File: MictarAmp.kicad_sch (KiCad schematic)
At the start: 8 parts, among them J1 AudioJack3, J2 AudioJack4, J3 AudioJack2, U1 LM386

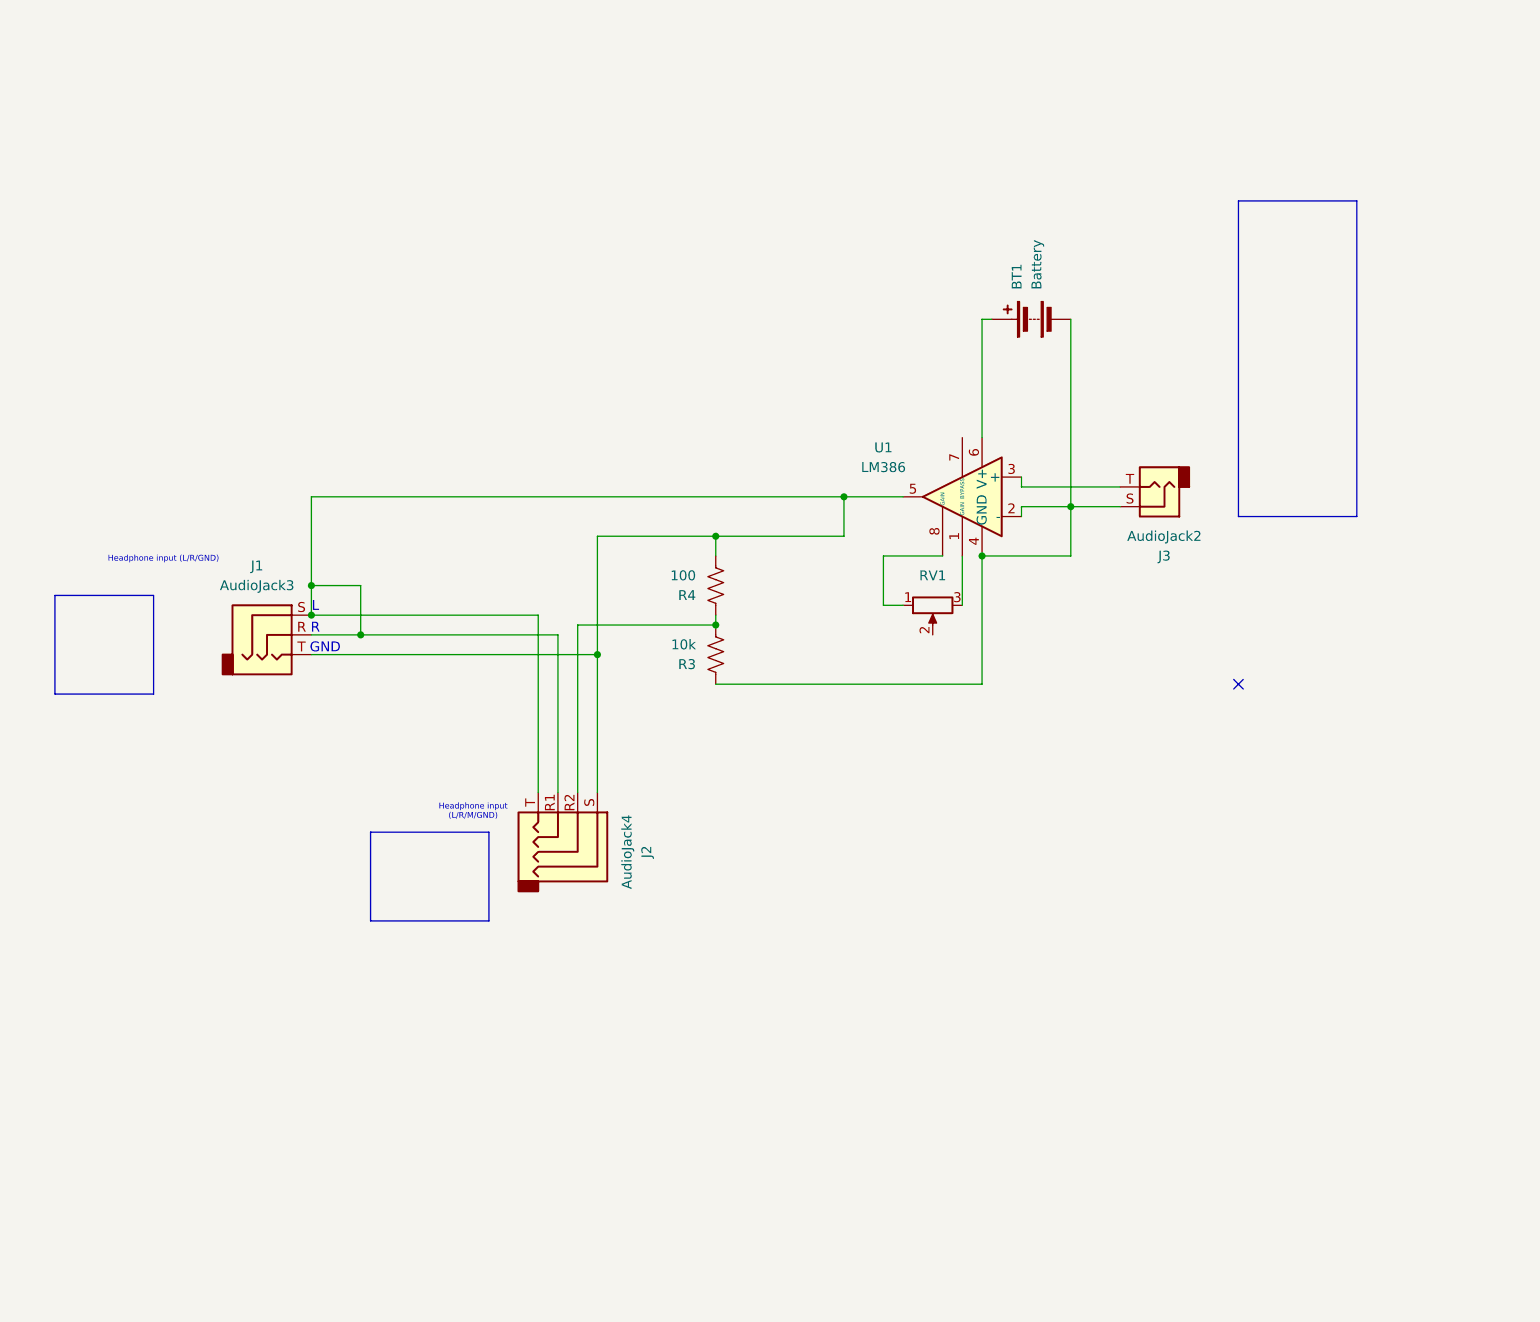
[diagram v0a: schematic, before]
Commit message: made a prototype of full version
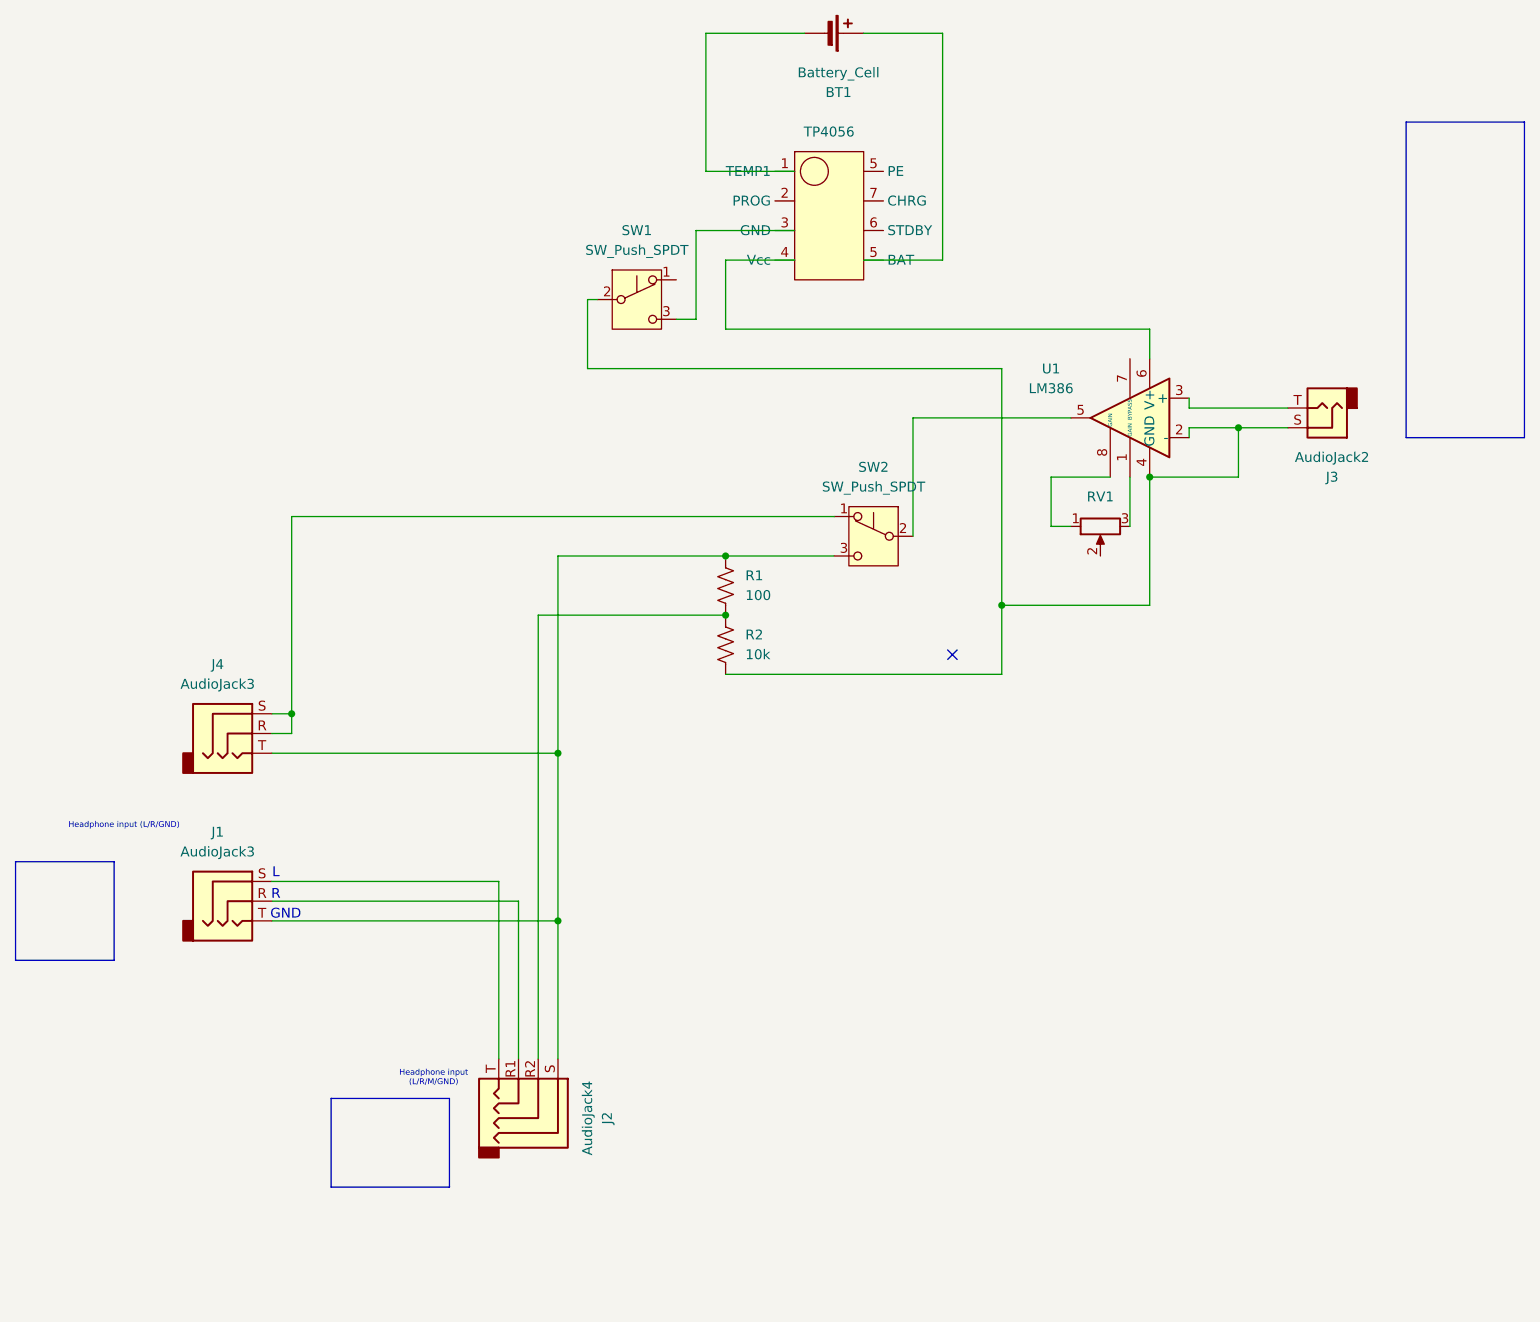
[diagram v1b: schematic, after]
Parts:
- removed BT1: Battery, symbol Device:Battery
- removed R3: 10k, symbol Device:R_US
- removed R4: 100, symbol Device:R_US
- added BT1: Battery_Cell, symbol Device:Battery_Cell
- added J4: AudioJack3, symbol Connector_Audio:AudioJack3
- added R1: 100, symbol Device:R_US
- added R2: 10k, symbol Device:R_US
- added SW1, SW2: SW_Push_SPDT, symbol Switch:SW_Push_SPDT
- added U2: TP4056, symbol Charging_modules:TP4056
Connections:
- net at J2.R2: now also R1.1, R2.2
- net at J3.S, U1.2 (-), U1.4 (GND): now also R2.1, SW1.2 (B)
- net at U1.6 (V+): now also U2.4 (Vcc)
- new net: J4.R, J4.S, SW2.1 (A)
- new net: J1.T, J2.S, J4.T, R1.2, SW2.3 (C)
- new net: SW2.2 (B), U1.5
- new net: BT1.1 (+), U2.5 (PE)
- new net: BT1.2 (-), U2.1 (TEMP1)
- new net: SW1.3 (C), U2.3 (GND)
- new net: J1.R, J2.R1
- new net: J1.S, J2.T
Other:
- moved on the sheet: J1, J2, J3, RV1, U1

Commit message: updated footprint on some components
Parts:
- BT1: footprint (none) -> Connector_PinHeader_1.00mm:PinHeader_1x02_P1.00mm_Vertical
- SW1, SW2, U1: footprint (none) -> Connector_PinHeader_1.00mm:PinHeader_2x03_P1.00mm_Vertical
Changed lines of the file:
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@@
 			)
 		)
-		(property "Footprint" ""
+		(property "Footprint" "Connector_PinHeader_1.00mm:PinHeader_2x03_P1.00mm_Vertical"
 			(at 170.18 92.71 0)
 			(effects
@@
 			)
 		)
-		(property "Footprint" ""
+		(property "Footprint" "Connector_PinHeader_1.00mm:PinHeader_1x02_P1.00mm_Vertical"
 			(at 165.354 27.94 90)
 			(effects
@@
 			)
 		)
-		(property "Footprint" ""
+		(property "Footprint" "Connector_PinHeader_1.00mm:PinHeader_2x03_P1.00mm_Vertical"
 			(at 139.7 62.23 0)
 			(effects
@@
 			)
 		)
-		(property "Footprint" ""
+		(property "Footprint" "Connector_PinHeader_1.00mm:PinHeader_2x03_P1.00mm_Vertical"
 			(at 200.66 74.93 0)
 			(effects
